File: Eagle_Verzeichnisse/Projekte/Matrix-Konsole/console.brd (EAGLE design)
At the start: 127 x 89.8 mm, 15 parts, among them J1 DIN5, J2 DIN5, J3 DIN5, J4 DIN5, X2 057-016-1

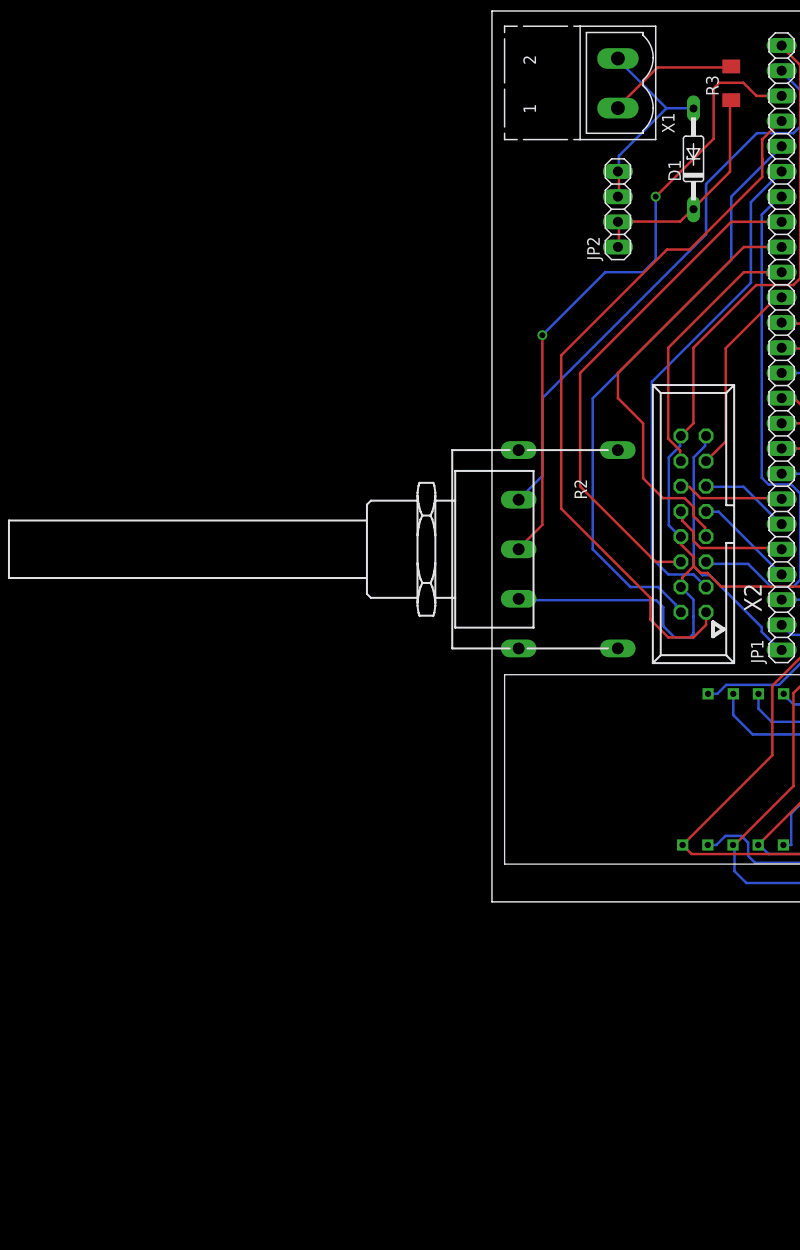
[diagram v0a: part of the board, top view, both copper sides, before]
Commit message: Added Spannungsregler
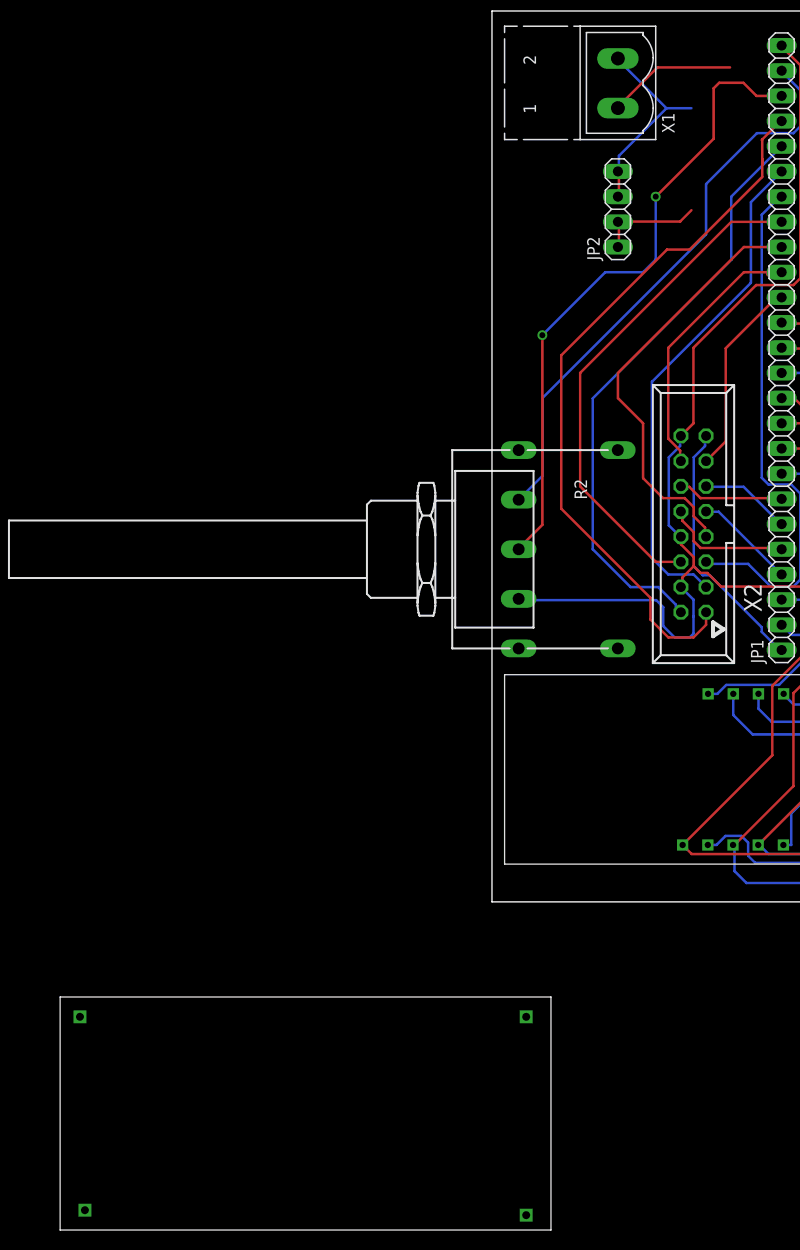
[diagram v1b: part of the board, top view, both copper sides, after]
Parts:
- removed D1: 5V, diode:DO35Z10
- removed R3: 10, resistor:M3516
- added U$1: SPGRGL_DEV, Spannungsregler:SPGRGL_PACK
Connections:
- removed net N$3: D1.C, JP2.1, JP2.2, R3.1
- new net N$1: JP2.1, JP2.2, U$1.OUT+
- new net N$8: JP2.3, JP2.4, U$1.OUT-
- net GND: now also U$1.IN-; no longer D1.A, JP2.3, JP2.4
- net VCC: now also U$1.IN+; no longer R3.2
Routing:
- net N$3: track 23.3 -> 0.00 mm
- net N$1: track 0.00 -> 10.5 mm
- net GND: track 20.9 -> 17.7 mm
- net N$8: track 0.00 -> 2.72 mm
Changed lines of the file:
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@@
 <layer number="2" name="Route2" color="1" fill="3" visible="no" active="no"/>
 <layer number="3" name="Route3" color="4" fill="3" visible="no" active="no"/>
+<layer number="4" name="Route4" color="1" fill="4" visible="no" active="no"/>
+<layer number="5" name="Route5" color="4" fill="4" visible="no" active="no"/>
+<layer number="6" name="Route6" color="1" fill="8" visible="no" active="no"/>
+<layer number="7" name="Route7" color="4" fill="8" visible="no" active="no"/>
+<layer number="8" name="Route8" color="1" fill="2" visible="no" active="no"/>
+<layer number="9" name="Route9" color="4" fill="2" visible="no" active="no"/>
+<layer number="10" name="Route10" color="1" fill="7" visible="no" active="no"/>
+<layer number="11" name="Route11" color="4" fill="7" visible="no" active="no"/>
+<layer number="12" name="Route12" color="1" fill="5" visible="no" active="no"/>
+<layer number="13" name="Route13" color="4" fill="5" visible="no" active="no"/>
 <layer number="14" name="Route14" color="1" fill="6" visible="no" active="no"/>
 <layer number="15" name="Route15" color="4" fill="6" visible="no" active="no"/>
@@
 <element name="7SEG1" library="seven_segment" package="7SEG_PACK" value="7SEG_DEV" x="54.61" y="1.27"/>
 <element name="7SEG2" library="seven_segment" package="7SEG_PACK" value="7SEG_DEV" x="1.27" y="1.27"/>
-<element name="D1" library="diode" package="DO35Z10" value="5V" x="20.32" y="72.39" rot="R90"/>
 <element name="J1" library="SparkFun-Connectors" package="DIN5-RA-PTH" value="DIN5" x="127" y="76.2" rot="R90">
 <attribute name="PROD_ID" value="CONN-09481" x="127" y="76.2" size="1.778" layer="27" rot="R90" display="off"/>
@@
 <attribute name="OC_NEWARK" value="unknown" x="-3.81" y="33.02" size="1.778" layer="27" rot="R270" display="off"/>
 </element>
-<element name="R3" library="resistor" package="M3516" value="10" x="24.13" y="80.01" rot="R90"/>
 <element name="U$2" library="max7219" package="SO24L" value="MAX7219CWG" x="53.34" y="27.94"/>
 <element name="X1" library="con-phoenix-500" package="MSTBV2" value="" x="12.7" y="80.01" rot="R90">
@@
 <attribute name="OC_NEWARK" value="unknown" x="20.32" y="35.56" size="1.778" layer="27" rot="R90" display="off"/>
 </element>
+<element name="U$1" library="Spannungsregler" package="SPGRGL_PACK" value="SPGRGL_DEV" x="-19.05" y="-24.13"/>
 </elements>
 <signals>
 <signal name="GND">
 <contactref element="X1" pad="2"/>
-<contactref element="JP2" pad="3"/>
-<contactref element="JP2" pad="4"/>
-<contactref element="D1" pad="A"/>
-<wire x1="12.8016" y1="71.0946" x2="12.8016" y2="68.58" width="0.254" layer="1"/>
-<wire x1="12.8016" y1="68.58" x2="12.7" y2="68.58" width="0.254" layer="1"/>
-<wire x1="12.8016" y1="71.0946" x2="12.7" y2="71.12" width="0.254" layer="1"/>
 <wire x1="17.6022" y1="77.4954" x2="20.1168" y2="77.4954" width="0.254" layer="16"/>
 <wire x1="12.8016" y1="82.296" x2="17.6022" y2="77.4954" width="0.254" layer="16"/>
-<wire x1="20.1168" y1="77.4954" x2="20.32" y2="77.47" width="0.254" layer="16"/>
 <wire x1="12.8016" y1="82.296" x2="12.7" y2="82.51" width="0.254" layer="16"/>
 <wire x1="12.8016" y1="72.6948" x2="12.8016" y2="71.3232" width="0.254" layer="16"/>
 <wire x1="17.6022" y1="77.4954" x2="12.8016" y2="72.6948" width="0.254" layer="16"/>
-<wire x1="12.8016" y1="71.3232" x2="12.7" y2="71.12" width="0.254" layer="16"/>
+<contactref element="U$1" pad="IN-"/>
+<wire x1="-41.05" y1="-33.63" x2="12.8016" y2="71.3232" width="0" layer="19" extent="16-16"/>
 </signal>
 <signal name="VCC">
 <contactref element="X1" pad="1"/>
-<contactref element="R3" pad="2"/>
 <wire x1="16.6878" y1="81.6102" x2="24.003" y2="81.6102" width="0.254" layer="1"/>
 <wire x1="12.8016" y1="77.724" x2="16.6878" y2="81.6102" width="0.254" layer="1"/>
-<wire x1="24.003" y1="81.6102" x2="24.13" y2="81.71" width="0.254" layer="1"/>
 <wire x1="12.8016" y1="77.724" x2="12.7" y2="77.51" width="0.254" layer="1"/>
+<contactref element="U$1" pad="IN+"/>
+<wire x1="-41.55" y1="-14.13" x2="12.7" y2="77.51" width="0" layer="19" extent="1-1"/>
 </signal>
 <signal name="SER1">
@@
 <wire x1="107.95" y1="55.88" x2="107.95" y2="42.07" width="0.254" layer="16"/>
 <wire x1="107.95" y1="42.07" x2="112" y2="38.02" width="0.254" layer="16"/>
-</signal>
-<signal name="N$3">
-<contactref element="JP2" pad="1"/>
-<contactref element="JP2" pad="2"/>
-<contactref element="R3" pad="1"/>
-<contactref element="D1" pad="C"/>
-<wire x1="12.8016" y1="65.8368" x2="12.8016" y2="63.5508" width="0.254" layer="1"/>
-<wire x1="12.8016" y1="63.5508" x2="12.7" y2="63.5" width="0.254" layer="1"/>
-<wire x1="12.8016" y1="65.8368" x2="12.7" y2="66.04" width="0.254" layer="1"/>
-<wire x1="24.003" y1="71.0946" x2="24.003" y2="78.1812" width="0.254" layer="1"/>
-<wire x1="20.3454" y1="67.437" x2="24.003" y2="71.0946" width="0.254" layer="1"/>
-<wire x1="24.003" y1="78.1812" x2="24.13" y2="78.31" width="0.254" layer="1"/>
-<wire x1="20.3454" y1="67.437" x2="20.32" y2="67.31" width="0.254" layer="1"/>
-<wire x1="18.9738" y1="66.0654" x2="12.8016" y2="66.0654" width="0.254" layer="1"/>
-<wire x1="20.1168" y1="67.2084" x2="18.9738" y2="66.0654" width="0.254" layer="1"/>
-<wire x1="12.8016" y1="66.0654" x2="12.7" y2="66.04" width="0.254" layer="1"/>
-<wire x1="20.1168" y1="67.2084" x2="20.32" y2="67.31" width="0.254" layer="1"/>
 </signal>
 <signal name="MEGA_GND">
@@
 <wire x1="22.352" y1="74.422" x2="16.51" y2="68.58" width="0.254" layer="1"/>
 </signal>
+<signal name="N$8">
+<contactref element="JP2" pad="3"/>
+<contactref element="JP2" pad="4"/>
+<wire x1="12.8016" y1="71.0946" x2="12.8016" y2="68.58" width="0.254" layer="1"/>
+<wire x1="12.8016" y1="68.58" x2="12.7" y2="68.58" width="0.254" layer="1"/>
+<wire x1="12.8016" y1="71.0946" x2="12.7" y2="71.12" width="0.254" layer="1"/>
+<contactref element="U$1" pad="OUT-"/>
+<wire x1="3.45" y1="-34.13" x2="12.7" y2="68.58" width="0" layer="19" extent="1-1"/>
+</signal>
+<signal name="N$1">
+<contactref element="JP2" pad="1"/>
+<contactref element="JP2" pad="2"/>
+<wire x1="12.8016" y1="65.8368" x2="12.8016" y2="63.5508" width="0.254" layer="1"/>
+<wire x1="12.8016" y1="63.5508" x2="12.7" y2="63.5" width="0.254" layer="1"/>
+<wire x1="12.8016" y1="65.8368" x2="12.7" y2="66.04" width="0.254" layer="1"/>
+<wire x1="18.9738" y1="66.0654" x2="12.8016" y2="66.0654" width="0.254" layer="1"/>
+<wire x1="20.1168" y1="67.2084" x2="18.9738" y2="66.0654" width="0.254" layer="1"/>
+<wire x1="12.8016" y1="66.0654" x2="12.7" y2="66.04" width="0.254" layer="1"/>
+<contactref element="U$1" pad="OUT+"/>
+<wire x1="3.45" y1="-14.13" x2="12.7" y2="63.5" width="0" layer="19" extent="1-1"/>
+</signal>
 </signals>

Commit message: Added Layout for console
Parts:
- added C1: 100n, eagle-ltspice:C0805
- moved U$1 197.2 mm to (93.2, 138.0)
- moved JP2 152.8 mm to (147.3, 139.7), turned to 270 degrees
- moved J4 151.7 mm to (199.4, 144.8)
- moved JP1 146.0 mm to (94.0, 182.9), turned to 0 degrees
- moved X1 113.0 mm to (12.7, 193.0)
- moved 7SEG2 109.2 mm to (110.5, 3.81)
- moved X2 93.0 mm to (96.5, 88.9), turned to 180 degrees
- moved J1 81.8 mm to (199.4, 114.3)
- moved J2 78.1 mm to (199.4, 83.8)
- moved J3 75.2 mm to (199.4, 53.3)
- moved U$2 59.7 mm to (105.4, 57.1)
- moved R1 47.1 mm to (105.4, 69.8), turned to 180 degrees
- moved R2 39.7 mm to (1.27, 72.4)
- moved 7SEG1 3.59 mm to (57.1, 3.81)
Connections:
- net 5V: now also C1.1
- net MEGA_GND: now also C1.2
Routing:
- net MEGA_A9: track 64.7 -> 236.4 mm
- net MEGA_GND: track 271.3 -> 428.9 mm, vias 0 -> 4
- net MAX_DIN: track 29.8 -> 186.7 mm, vias 0 -> 1
- net MAX_LOAD: track 34.7 -> 155.5 mm, vias 1 -> 3
- net 5V: track 276.3 -> 383.3 mm, vias 1 -> 7
- net MATRIX_B: track 12.8 -> 110.1 mm, vias 0 -> 2
- net MATRIX_D: track 10.7 -> 104.6 mm
- net SER4: track 109.3 -> 201.8 mm
- net MATRIX_C: track 9.17 -> 101.3 mm, vias 0 -> 2
- net MATRIX_A: track 10.2 -> 102.3 mm
- net MAX_CLK: track 42.3 -> 133.4 mm
- net MATRIX_LAT: track 29.3 -> 108.4 mm, vias 0 -> 2
- net MATRIX_CLK: track 21.6 -> 99.3 mm, vias 0 -> 2
- net MATRIX_OE: track 26.3 -> 102.3 mm
- net GND: track 17.7 -> 92.4 mm
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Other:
- board size 127 x 89.8 mm -> 200.6 x 200.3 mm

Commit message: Added Bestellnumnmern to Stückliste, Added Bohrungen to console-layout
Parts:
- moved X1 96.5 mm to (12.7, 96.5)
- moved U$1 77.6 mm to (15.6, 137.7), turned to 90 degrees
- moved JP2 12.7 mm to (160.0, 139.7)
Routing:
- net N$1: track 45.2 -> 214.3 mm
- net N$8: track 42.8 -> 188.5 mm
- net GND: track 92.4 -> 27.6 mm
- net VCC: track 74.7 -> 41.1 mm
- net MEGA_A9: track 236.4 -> 256.0 mm
- net MATRIX_B: track 110.1 -> 128.4 mm
- net SER2: track 185.0 -> 202.4 mm
- net CLK: track 222.6 -> 238.8 mm
- net MATRIX_OE: track 102.3 -> 117.8 mm
- net MATRIX_CLK: track 99.3 -> 114.1 mm
- net MAX_LOAD: track 155.5 -> 166.8 mm
- net 5V: track 383.3 -> 393.8 mm
- net MATRIX_R1: track 98.1 -> 105.5 mm
- net DIG6: track 62.4 -> 68.5 mm
- net MAX_DIN: track 186.7 -> 192.2 mm
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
